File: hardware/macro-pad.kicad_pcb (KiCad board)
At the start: 2 copper layers, 94 x 68 mm, 43 parts, among them J1 USB_C_Receptacle_USB2.0, SW1 PEC12R-4025F-S0024, SW2 MX1A-G1NA, SW3 MX1A-G1NA, SW4 MX1A-G1NA, SW5 MX1A-G1NA, U1 MIC5317-3.3ZD5-TR, U2 RP2040, U3 W25Q128JVSIQ, Y1 ABLS-12.000MHZ-B4-T

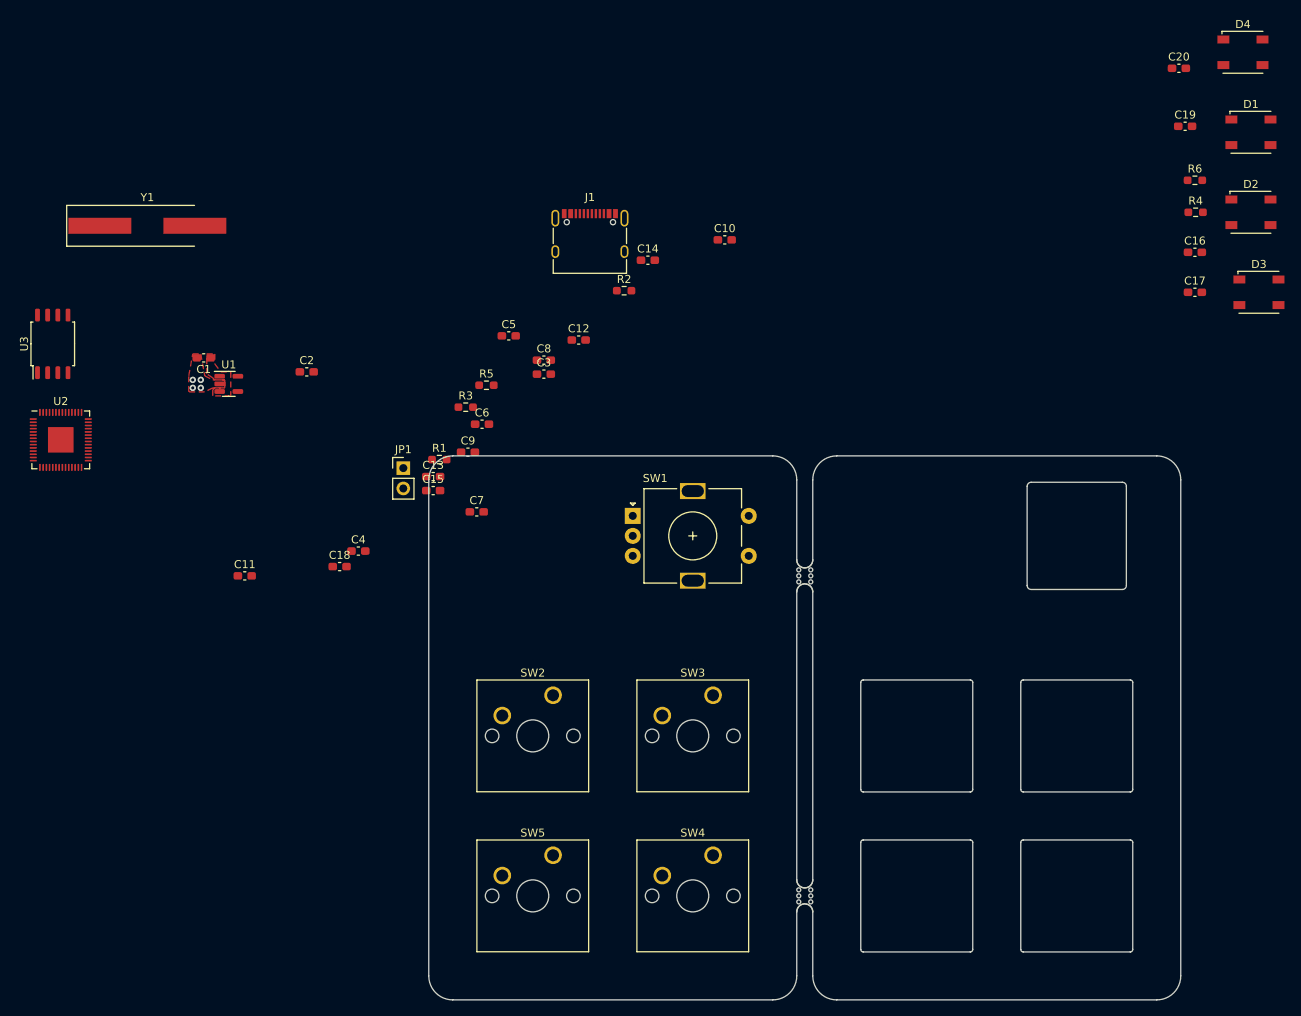
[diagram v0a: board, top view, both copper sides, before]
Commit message: Resized PCB and added some comonents
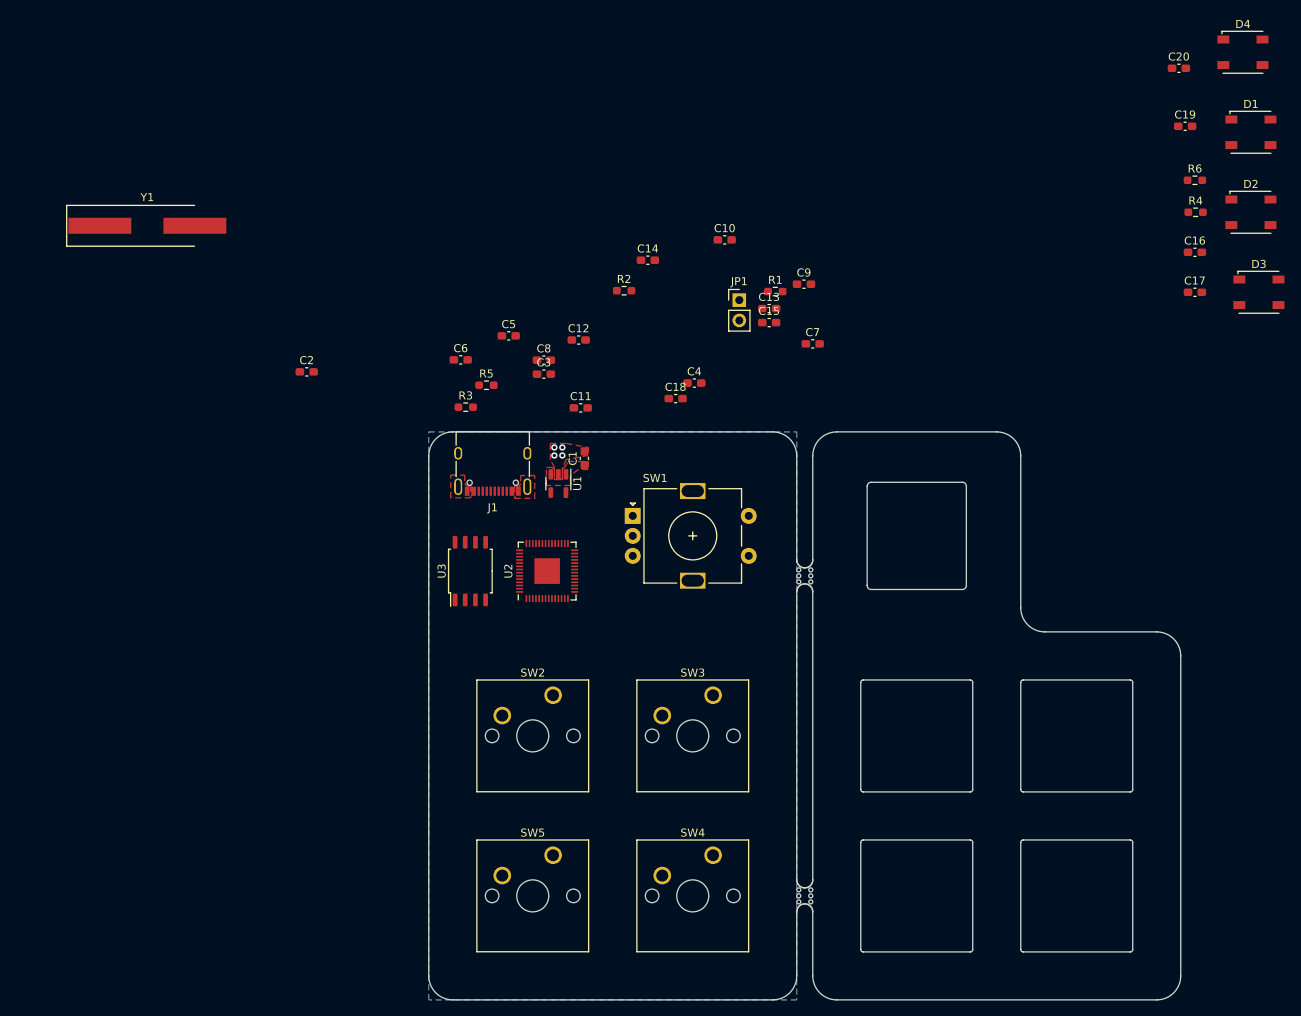
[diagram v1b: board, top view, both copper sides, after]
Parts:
- moved U2 63.0 mm to (111.8, 89.4), turned to 90 degrees
- moved U3 59.4 mm to (102.2, 89.4)
- moved C1 49.2 mm to (116.5, 75.3), turned to 90 degrees
- moved C13 47.0 mm to (139.6, 56.6)
- moved C15 47.0 mm to (139.6, 58.3)
- moved C11 47.0 mm to (116.0, 69.0)
- moved C18 47.0 mm to (127.9, 67.8)
- moved C7 47.0 mm to (145.0, 61.0)
- moved C9 47.0 mm to (143.9, 53.5)
- moved JP1 47.0 mm to (135.8, 55.5)
- moved R1 47.0 mm to (140.3, 54.5)
- moved C4 47.0 mm to (130.2, 65.9)
- moved U1 43.0 mm to (113.2, 78.5), turned to -90 degrees
- moved J1 29.9 mm to (105.0, 75.8), turned to 180 degrees
- moved C6 8.47 mm to (101.0, 63.0)
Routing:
- added copper zone on B.Cu, net GND
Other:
- board size 94 x 68 mm -> 94 x 71 mm

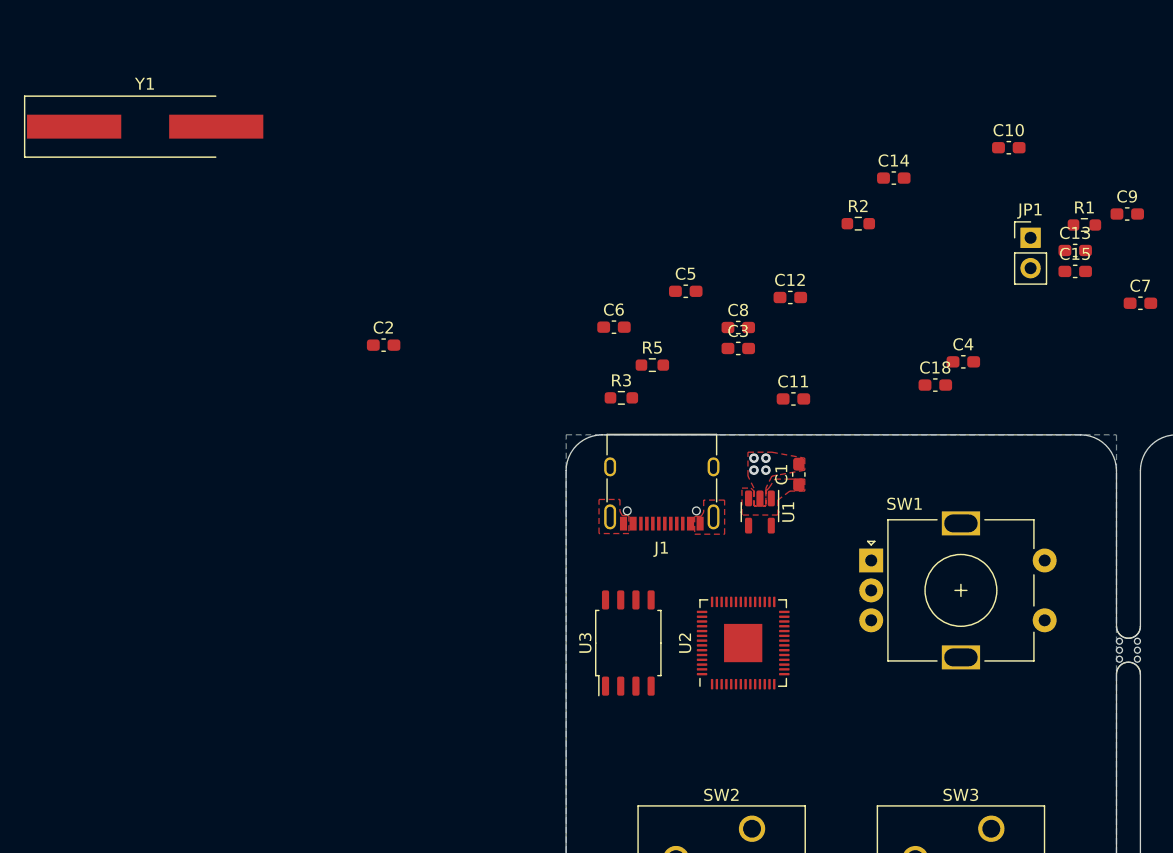
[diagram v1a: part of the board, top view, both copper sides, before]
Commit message: Completed power section
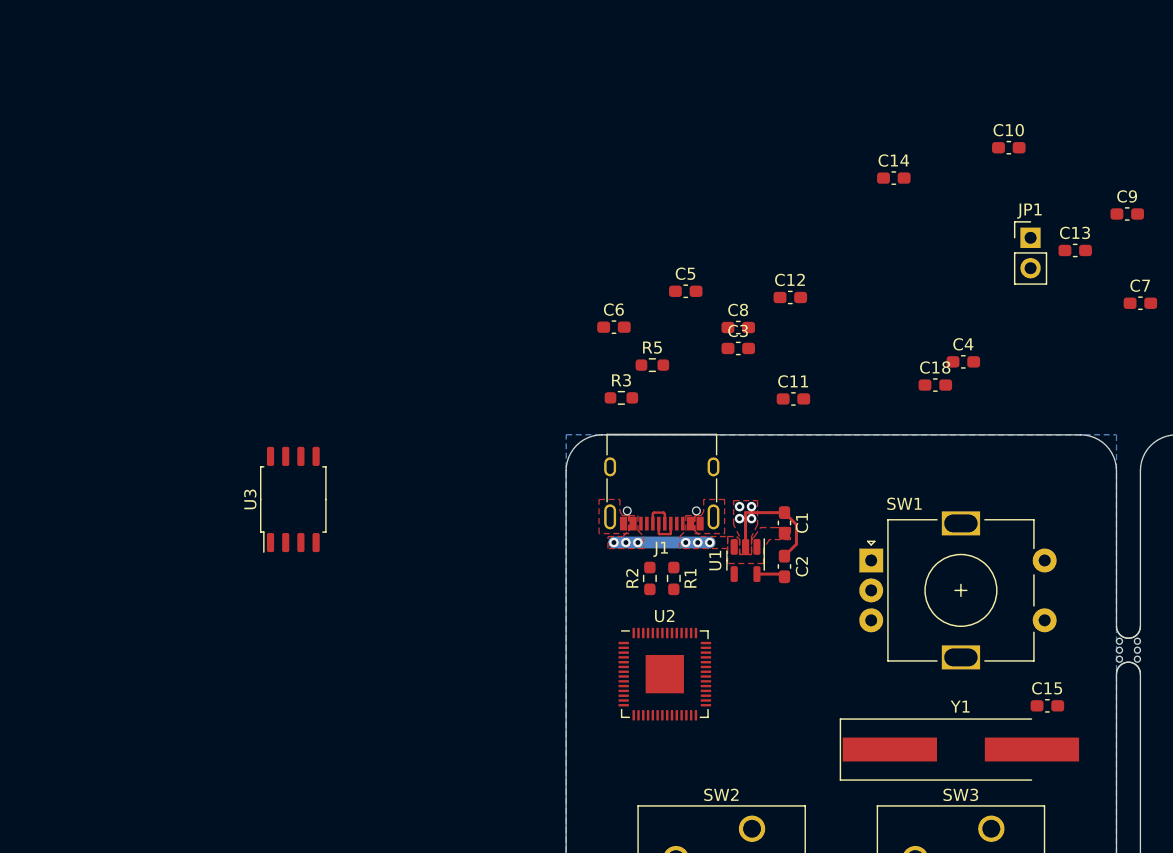
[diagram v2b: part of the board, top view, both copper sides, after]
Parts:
- moved Y1 85.8 mm to (130.0, 98.3)
- moved R1 45.3 mm to (106.0, 84.0), turned to -90 degrees
- moved C2 38.3 mm to (115.2, 83.0), turned to 90 degrees
- moved C15 36.4 mm to (137.2, 94.7)
- moved R2 34.4 mm to (104.0, 84.0), turned to 90 degrees
- moved U3 30.5 mm to (74.2, 77.4)
- moved U2 7.05 mm to (105.2, 92.0), turned to 0 degrees
- moved C1 4.22 mm to (115.2, 79.4)
- moved U1 4.22 mm to (112.0, 82.5)
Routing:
- net GND: track 0.00 -> 10.6 mm
- net +5V: track 0.00 -> 8.00 mm, vias 0 -> 6
- net /D_{USB}-: track 0.00 -> 2.73 mm
- net /D_{USB}+: track 0.00 -> 2.69 mm
- net +3V3: track 0.00 -> 2.39 mm

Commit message: Wired swicthes to be pulled down if actived instead of up
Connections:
- SW1 pad C: +3V3 -> GND
- SW1 pad S1: +3V3 -> GND
- SW2 pad 1: +3V3 -> GND
- SW3 pad 1: +3V3 -> GND
- SW4 pad 1: +3V3 -> GND
- SW5 pad 1: +3V3 -> GND
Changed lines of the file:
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@@
       (net 24 "/R_{B}") (pinfunction "B") (pintype "passive"))
     (pad "C" thru_hole circle (at 0 2.5) (size 2 2) (drill 1) (layers *.Cu *.Mask)
-      (net 3 "+3V3") (pinfunction "C") (pintype "passive"))
+      (net 2 "GND") (pinfunction "C") (pintype "passive"))
     (pad "MP" thru_hole rect (at 7.5 8.1) (size 3.2 2) (drill oval 2.8 1.5) (layers *.Cu *.Mask))
     (pad "MP" thru_hole rect (at 7.5 -3.1) (size 3.2 2) (drill oval 2.8 1.5) (layers *.Cu *.Mask))
     (pad "S1" thru_hole circle (at 14.5 5) (size 2 2) (drill 1) (layers *.Cu *.Mask)
-      (net 3 "+3V3") (pinfunction "S1") (pintype "passive"))
+      (net 2 "GND") (pinfunction "S1") (pintype "passive"))
     (pad "S2" thru_hole circle (at 14.5 0) (size 2 2) (drill 1) (layers *.Cu *.Mask)
       (net 25 "/R_{BTN}") (pinfunction "S2") (pintype "passive"))
@@
     (pad "" np_thru_hole circle (at 2.54 5.08) (size 1.7 1.7) (drill 1.7) (layers *.Cu *.Mask))
     (pad "1" thru_hole circle (at 0 0) (size 2.2 2.2) (drill 1.5) (layers *.Cu *.Mask)
-      (net 3 "+3V3") (pinfunction "1") (pintype "passive"))
+      (net 2 "GND") (pinfunction "1") (pintype "passive"))
     (pad "2" thru_hole circle (at -6.35 2.54) (size 2.2 2.2) (drill 1.5) (layers *.Cu *.Mask)
       (net 26 "/SW_{1}") (pinfunction "2") (pintype "passive"))
@@
     (pad "" np_thru_hole circle (at -7.62 5.08) (size 1.7 1.7) (drill 1.7) (layers *.Cu *.Mask))
     (pad "1" thru_hole circle (at 0 0) (size 2.2 2.2) (drill 1.5) (layers *.Cu *.Mask)
-      (net 3 "+3V3") (pinfunction "1") (pintype "passive"))
+      (net 2 "GND") (pinfunction "1") (pintype "passive"))
     (pad "2" thru_hole circle (at -6.35 2.54) (size 2.2 2.2) (drill 1.5) (layers *.Cu *.Mask)
       (net 28 "/SW_{3}") (pinfunction "2") (pintype "passive"))
@@
     (pad "" np_thru_hole circle (at -7.62 5.08) (size 1.7 1.7) (drill 1.7) (layers *.Cu *.Mask))
     (pad "1" thru_hole circle (at 0 0) (size 2.2 2.2) (drill 1.5) (layers *.Cu *.Mask)
-      (net 3 "+3V3") (pinfunction "1") (pintype "passive"))
+      (net 2 "GND") (pinfunction "1") (pintype "passive"))
     (pad "2" thru_hole circle (at -6.35 2.54) (size 2.2 2.2) (drill 1.5) (layers *.Cu *.Mask)
       (net 29 "/SW_{4}") (pinfunction "2") (pintype "passive"))
@@
     (pad "" np_thru_hole circle (at -2.54 5.08) (size 4 4) (drill 4) (layers *.Cu *.Mask))
     (pad "1" thru_hole circle (at 0 0) (size 2.2 2.2) (drill 1.5) (layers *.Cu *.Mask)
-      (net 3 "+3V3") (pinfunction "1") (pintype "passive"))
+      (net 2 "GND") (pinfunction "1") (pintype "passive"))
     (pad "2" thru_hole circle (at -6.35 2.54) (size 2.2 2.2) (drill 1.5) (layers *.Cu *.Mask)
       (net 27 "/SW_{2}") (pinfunction "2") (pintype "passive"))

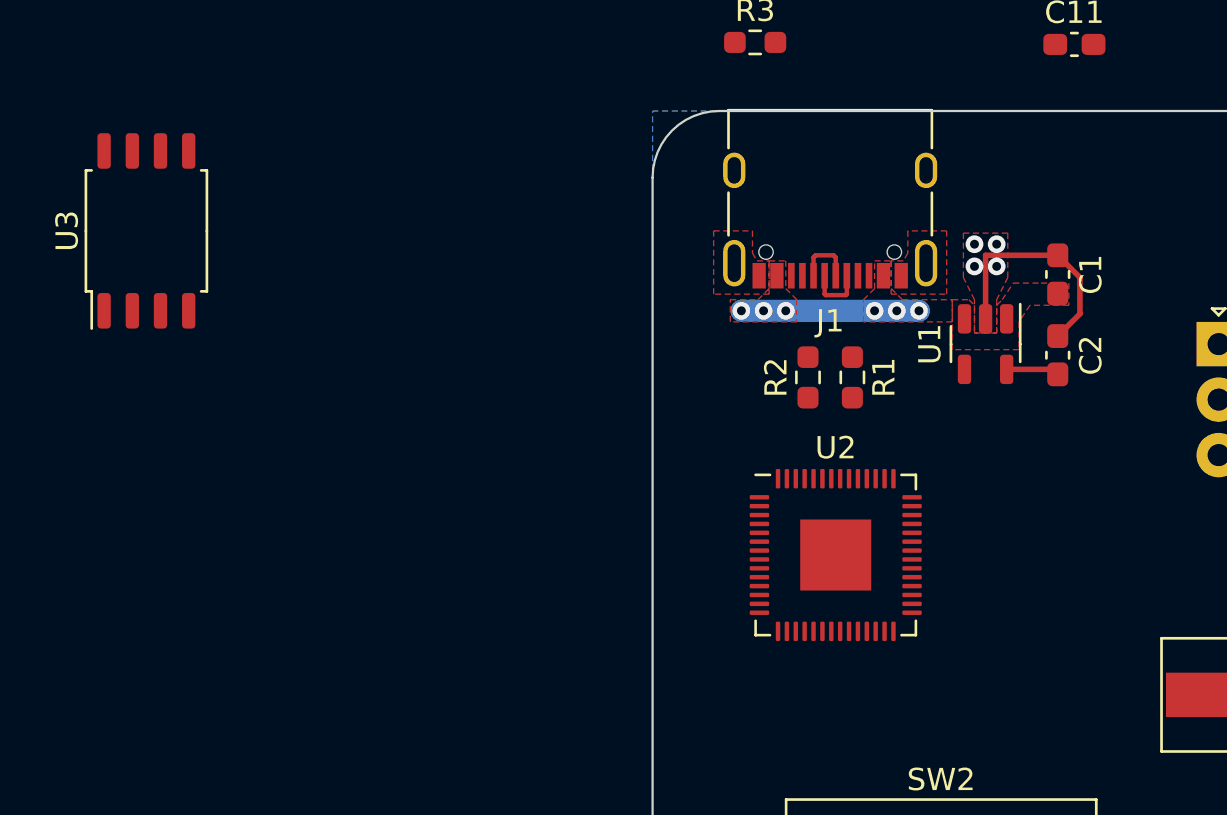
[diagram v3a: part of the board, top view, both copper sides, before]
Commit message: Corrected SMD LED footprint
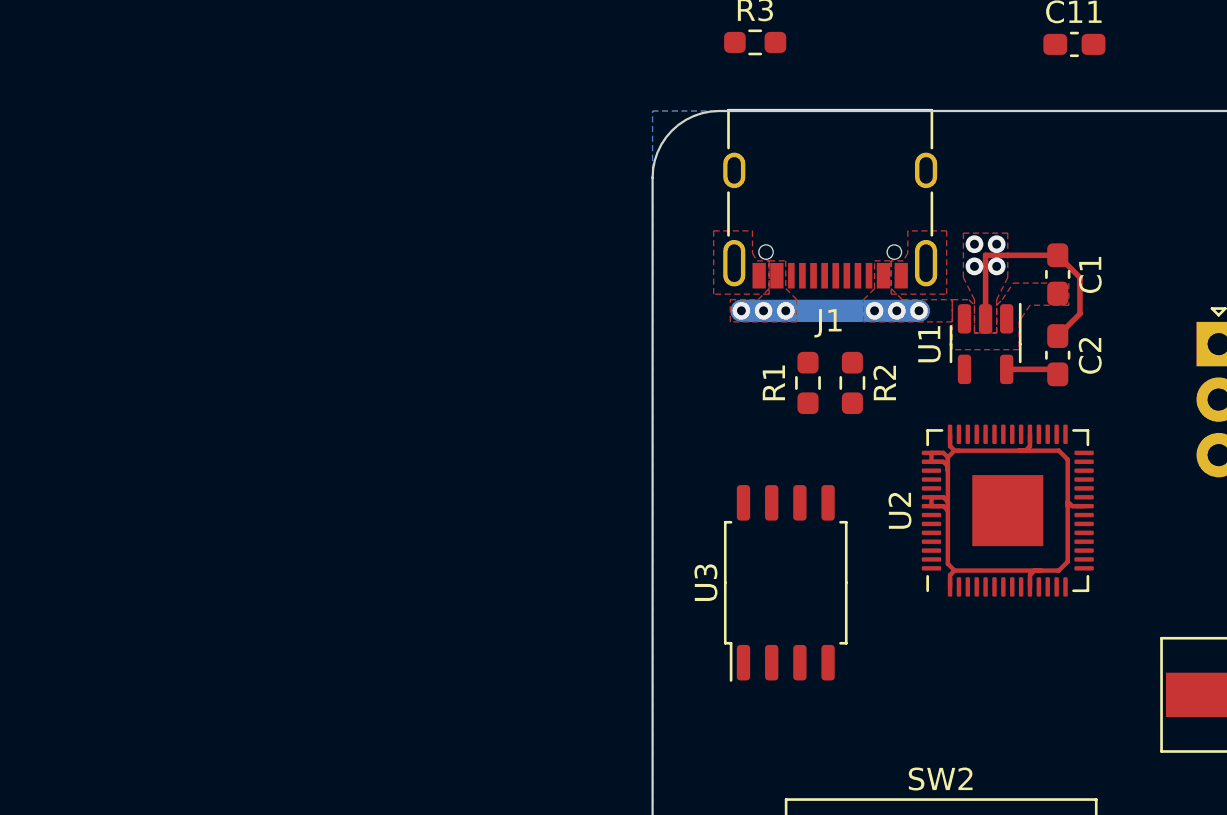
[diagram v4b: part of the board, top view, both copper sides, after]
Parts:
- moved U3 32.9 mm to (103.0, 93.2)
- moved U2 8.00 mm to (113.0, 90.0), turned to 90 degrees
- moved R1 2.02 mm to (104.0, 84.2)
- moved R2 2.02 mm to (106.0, 84.2)
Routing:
- net +3V3: track 2.39 -> 32.6 mm
- net /D_{USB}-: track 2.73 -> 0.00 mm
- net /D_{USB}+: track 2.69 -> 0.00 mm
